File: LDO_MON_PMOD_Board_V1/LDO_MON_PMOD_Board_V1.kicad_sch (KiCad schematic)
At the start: 49 parts, among them J1 Conn_01x03, P1 PMOD-Device-x2-Type-Generic-A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, P2 PMOD-Device-x2-Type-Generic-A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, U1 LT3074AV#PBF, U2 LT3074AV#PBF

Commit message: Schematic and PCB Updates.
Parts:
- added C28, C29, C30, C31, C33, C47: 100n, Capacitor_SMD:C_0402_1005Metric, symbol Device:C_Small
- added C32: 4u7, Capacitor_SMD:C_0603_1608Metric, symbol Device:C_Small
- added C34, C37, C40, C43: 47n, Capacitor_SMD:C_0402_1005Metric, symbol Device:C_Small
- added C35, C36, C38, C39, C41, C42, C44, C45: 4n7, Capacitor_SMD:C_0402_1005Metric, symbol Device:C_Small
- added C46: 10n, Capacitor_SMD:C_0402_1005Metric, symbol Device:C_Small
- added C48: 10u, Capacitor_SMD:C_0603_1608Metric, symbol Device:C_Small
- added C49: 1u, Capacitor_SMD:C_0402_1005Metric, symbol Device:C_Small
- added J2: 2-Pin Harwin, Connector_PinHeader_2.54mm:PinHeader_1x02_P2.54mm_Vertical, symbol Connector_Generic:Conn_01x02
- added J3: Conn_01x04, Connector_Phoenix_MC:PhoenixContact_MC_1,5_4-G-3.5_1x04_P3.50mm_Horizontal, symbol Connector_Generic:Conn_01x04
- added JP1, JP2, JP3: SolderJumper_3_Open, Jumper:SolderJumper-3_P1.3mm_Open_RoundedPad1.0x1.5mm, symbol Jumper:SolderJumper_3_Open
- added R17, R20, R21, R23, R24, R25, R37, R38: 10k, Resistor_SMD:R_0402_1005Metric, symbol Device:R
- added R18, R19: 1k, Resistor_SMD:R_0402_1005Metric, symbol Device:R
- added R26, R36, R8: 0R, Resistor_SMD:R_0402_1005Metric, symbol Device:R
- added R27, R28, R29, R30, R31, R32, R33, R34: 4k99, Resistor_SMD:R_0402_1005Metric, symbol Device:R
- added R35, R39: 15mR, Resistor_SMD:R_2512_6332Metric, symbol Device:R
- added R40: 100R, Resistor_SMD:R_0402_1005Metric, symbol Device:R
- added R9: 50k, Resistor_SMD:R_0402_1005Metric, symbol Device:R
- added U3: MAX6373, Package_TO_SOT_SMD:SOT-23-8, symbol Power_Supervisor:MAX6373
- added U4: 74LVC1G175, Package_TO_SOT_SMD:SOT-563, symbol 74xGxx:74LVC1G175
- added U5: PAC1944x-x4MX, Package_DFN_QFN:VQFN-16-1EP_3x3mm_P0.5mm_EP1.1x1.1mm, symbol Sensor_Energy:PAC1944x-x4MX
- added U6: 74LVC1G08, Package_TO_SOT_SMD:Texas_R-PDSO-G5_DCK-5, symbol 74xGxx:74LVC1G08
- added U7: AD5272BCP, Package_CSP:LFCSP-WD-10-1EP_3x3mm_P0.5mm_EP1.64x2.38mm, symbol Potentiometer_Digital:AD5272BCP
- C1, C14, C15, C17, C18, C19, C20, C21, C23, C24, C26, C27, C5: footprint (none) -> Capacitor_SMD:C_0402_1005Metric
- C10, C12, C4, C7: footprint (none) -> Capacitor_SMD:C_1210_3225Metric
- C11, C13, C16, C2, C22, C25, C3, C8, C9: footprint (none) -> Capacitor_SMD:C_0603_1608Metric
- C6: footprint (none) -> Capacitor_SMD:CP_Elec_8x10
- J1: value Conn_01x03 -> 3-Pin Harwin; footprint Connector:Tag-Connect_TC2030-IDC-FP_2x03_P1.27mm_Vertical -> Connector_PinHeader_2.54mm:PinHeader_1x03_P2.54mm_Vertical
- P1, P2: footprint pmod-conn_6x2:pmod_pin_array_6x2 -> klib_connectors:pmod_pin_array_6x2
- R1, R11, R12, R3, R5: footprint (none) -> Resistor_SMD:R_0402_1005Metric
- R13: value 1k -> 69k8; footprint (none) -> Resistor_SMD:R_0402_1005Metric
- R14, R2: value 1k -> 261k; footprint (none) -> Resistor_SMD:R_0402_1005Metric
- R15, R16: footprint (none) -> Resistor_SMD:R_2512_6332Metric
- R4: value 1k -> 47k5; footprint (none) -> Resistor_SMD:R_0402_1005Metric
- R6, R7: value 10k -> 4k7; footprint (none) -> Resistor_SMD:R_0402_1005Metric
- TP1, TP2, TP3, TP4: footprint Package_TO_SOT_SMD:SOT-23-5 -> TestPoint:TestPoint_Pad_1.0x1.0mm
- U1, U2: footprint Package_DFN_QFN:DFN-6-1EP_2x2mm_P0.5mm_EP0.6x1.37mm -> klib_logic:LT3074AV#PBF
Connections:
- net 3V3_PMOD: now also C29.1, C30.1, C31.1, C32.1, C33.1, C46.1, C47.1, C48.1, J2.1 (Pin_1), JP1.3 (B), JP2.3 (B), JP3.3 (B), R17.1, R18.1, R23.1, R24.1, R25.1, R37.1, U3.8 (VCC), U4.3 (D), U4.5 (VCC), U5.2 (V_{DD}), U6.5 (VCC), U7.1 (VDD)
- net ENABLE: now also J2.2 (Pin_2), R18.2, R40.1, U6.4; no longer U2.22 (EN)
- net EXT_VBIAS: now also J3.1 (Pin_1)
- net GND: now also C28.2, C29.2, C30.2, C31.2, C32.2, C33.2, C35.2, C36.2, C38.2, C39.2, C41.2, C42.2, C44.2, C45.2, C46.2, C47.2, C48.2, C49.2, J3.4 (Pin_4), JP1.1 (A), JP2.1 (A), JP3.1 (A), R19.2, R20.2, R21.2, R26.2, R38.2, R8.2, R9.2, U3.2 (GND), U4.2 (GND), U5.17 (EP), U5.3 (GND), U6.3 (GND), U7.11 (VSS), U7.3 (W), U7.4 (VSS), U7.6 (GND)
- net OUT_1: now also R28.2
- net OUT_2: now also R29.2
- net SCL: now also U5.4 (SCL), U7.9 (SCL)
- net SDA: now also U5.5 (SDA), U7.8 (SDA)
- net SET_RES_NODE: now also R36.2, R8.1
- net CNTRL: now reaches P2.7 (P7)
- net CNTRL: now also R20.1, U6.2
- net WDI: now reaches P2.8 (P8)
- net WDI: now also R19.1, U3.1 (WDI), U4.1 (C)
- net PAC_EN: now reaches P1.1 (P1)
- net PAC_EN: now also R23.2, U5.16 (~{PWRDN})
- net SLOW: now reaches P1.2 (P2)
- net SLOW: now also R24.2, U5.1 (SLOW)
- net GPIO: now reaches P1.3 (P3)
- net GPIO: now also R25.2, U5.15 (GPIO)
- net DP_RST_N: now reaches P1.4 (P4)
- net DP_RST_N: now also R37.2, U7.7 (~{RESET})
- net V_COMB renamed SENSE_1_N
- net SENSE_1_N: now also R27.2, R30.2, R31.2, R39.1
- net V_IN renamed SENSE_4_N
- net SENSE_4_N: now also R34.2, R35.1
- new net: C37.1, C38.1, R29.1, U5.13 (SENSE2+)
- new net: C37.2, C39.1, R30.1, U5.14 (SENSE2-)
- new net: R38.1, U7.10 (ADDR)
- new net: R36.1, R9.1, U7.2 (A)
- new net: C49.1, U7.5 (EXT_CAP)
- new net: C28.1, R17.2, U3.7 (~{WDO}), U4.6 (~{CLR})
- new net: R40.2, U2.22 (EN)
- new net: C43.1, C44.1, R33.1, U5.10 (SENSE4+)
- new net: C34.2, C36.1, R27.1, U5.12 (SENSE1-)
- new net: C34.1, C35.1, R28.1, U5.11 (SENSE1+)
- new net: C40.2, C42.1, R32.1, U5.7 (SENSE3-)
- new net: JP2.2 (C), U3.5 (SET1)
- new net: R21.1, U4.4 (Q), U6.1
- new net: C43.2, C45.1, R34.1, U5.9 (SENSE4-)
- new net: JP3.2 (C), U3.6 (SET2)
- new net: C40.1, C41.1, R31.1, U5.8 (SENSE3+)
- new net: JP1.2 (C), U3.4 (SET0)
- new net: R26.1, U5.6 (ADDRSEL)
- new net SENSE_3_N: J3.2 (Pin_2), R32.2, R39.2
- new net SENSE_4_P: J3.3 (Pin_3), R33.2, R35.2
- no-connect marks 2 -> 9
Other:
- note added: "ADDRESS: 0x10"
- note added: "ADDRESS: 0x2F"
- note added: "ADDRESS: 0x6D"
- note added: "ADDRESS: 0x6F"
- note added: "DNF"
- note added: "LOCATE CLOSE TO REGULATORS"
- note added: "NOTE: AD5272 VERSION - 50K NOMINAL RESISTANCE"
- note added: "WATCHDOG CIRCUIT DECOUPLING"
- note added: "WSL25122L000FED"
- note added: "WSL2512R0150FEA"
- moved on the sheet: C1, C10, C11, C12, C13, C14, C15, C16, C17, C18, C19, C2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

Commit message: Schematic/PCB Updates.
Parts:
- removed P2: PMOD-Device-x2-Type-Generic-Alt, klib_connectors:pmod_pin_array_6x2, symbol klib_connectors:PMOD-Device-x2-Type-Generic-Alt
- added C50: 47u, Capacitor_SMD:C_1210_3225Metric, symbol Device:C_Small
- U4: footprint Package_TO_SOT_SMD:SOT-563 -> Package_TO_SOT_SMD:SOT-23-6
- U6: footprint Package_TO_SOT_SMD:Texas_R-PDSO-G5_DCK-5 -> Package_TO_SOT_SMD:Texas_R-PDSO-N5_DRL-5
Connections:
- net ALERT_N: now also P1.3 (P3)
- net CNTRL: now also P1.9 (P9)
- net GND: now also C50.2
- net GPIO: no longer P1.3 (P3)
- net SCL: now also P1.7 (P7)
- net SDA: now also P1.8 (P8)
- net SENSE_4_N: now also C50.1
- net WDI: now also P1.10 (P10)
- no-connect marks 9 -> 2
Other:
- moved on the sheet: C22, C23, C24, C46, C47, C48, C49, C6, C7, C8, J1, R36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

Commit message: PCB Updates.
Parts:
- added C51, C52: 100n, Capacitor_SMD:C_0402_1005Metric, symbol Device:C_Small
- added D1, D2: LED, LED_SMD:LED_0402_1005Metric, symbol Device:LED
- added Q1: MMBT3904, Package_TO_SOT_SMD:SOT-23, symbol Transistor_BJT:MMBT3904
- added R10, R41, R43: 4k7, Resistor_SMD:R_0402_1005Metric, symbol Device:R
- added R22: 200k, Resistor_SMD:R_0402_1005Metric, symbol Device:R
- added R42, R44: 1k, Resistor_SMD:R_0402_1005Metric, symbol Device:R
- added U8: PCA9306, Package_SO:VSSOP-8_2.3x2mm_P0.5mm, symbol Interface:PCA9306
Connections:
- net 3V3_PMOD: now also C52.1, D1.2 (A), D2.2 (A), R10.1, R41.1, U8.2 (VREF1)
- net BIAS: now also R22.1
- net CNTRL: now also P1.4 (P4); no longer P1.9 (P9)
- net DP_RST_N: now also P1.7 (P7); no longer P1.4 (P4)
- net ENABLE: now also R43.1
- net GND: now also C51.2, C52.2, Q1.2 (E), R42.2, U8.1 (GND)
- net SCL: now also P1.8 (P8), R10.2, U8.3 (SCL1); no longer P1.7 (P7), R6.2, U1.4 (SCL), U2.4 (SCL)
- net SDA: now also P1.9 (P9), R41.2, U8.4 (SDA1); no longer P1.8 (P8), R7.2, U1.5 (SDA), U2.5 (SDA)
- net SENSE_2_P_FILT: now reaches C37.1, C38.1, R29.1
- net SENSE_2_P_FILT: now also U5.8 (SENSE3+); no longer U5.13 (SENSE2+)
- net SENSE_2_N_FILT: now reaches C37.2, C39.1, R30.1
- net SENSE_2_N_FILT: now also U5.7 (SENSE3-); no longer U5.14 (SENSE2-)
- net SENSE_4_P_FILT: now reaches C43.1, C44.1, R33.1
- net SENSE_4_P_FILT: now also U5.13 (SENSE2+); no longer U5.10 (SENSE4+)
- net SENSE_1_N_FILT: now reaches C34.2, C36.1, R27.1
- net SENSE_1_N_FILT: now also U5.9 (SENSE4-); no longer U5.12 (SENSE1-)
- net SENSE_1_P_FILT: now reaches C34.1, C35.1, R28.1
- net SENSE_1_P_FILT: now also U5.10 (SENSE4+); no longer U5.11 (SENSE1+)
- net SENSE_3_N_FILT: now reaches C40.2, C42.1, R32.1
- net SENSE_3_N_FILT: now also U5.12 (SENSE1-); no longer U5.7 (SENSE3-)
- net SENSE_4_N_FILT: now reaches C43.2, C45.1, R34.1
- net SENSE_4_N_FILT: now also U5.14 (SENSE2-); no longer U5.9 (SENSE4-)
- net SENSE_3_P_FILT: now reaches C40.1, C41.1, R31.1
- net SENSE_3_P_FILT: now also U5.11 (SENSE1+); no longer U5.8 (SENSE3+)
- new net: D1.1 (K), R42.1
- new net: Q1.1 (B), R43.2
- new net: D2.1 (K), R44.1
- new net: Q1.3 (C), R44.2
- new net: C51.1, R22.2, U8.7 (VREF2), U8.8 (EN)
- new net SCL_HV: R6.2, U1.4 (SCL), U2.4 (SCL), U8.6 (SCL2)
- new net SDA_HV: R7.2, U1.5 (SDA), U2.5 (SDA), U8.5 (SDA2)
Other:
- moved on the sheet: C34, C35, C36, C37, C38, C39, C40, C41, C42, C43, C44, C45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

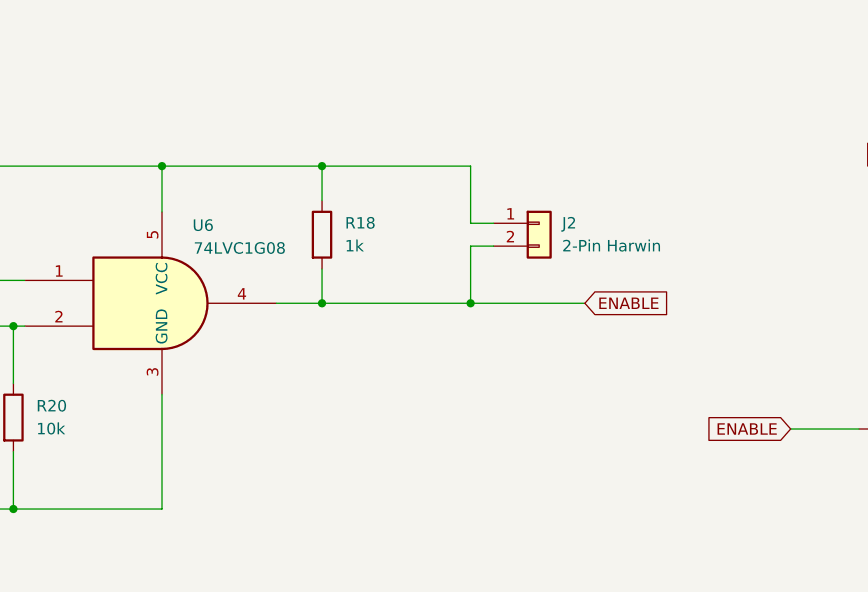
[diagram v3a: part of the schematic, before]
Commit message: Fixed problem with watchdog enable bypass. Updated schematic/PCB/gerbers. No change to placement or BOM.
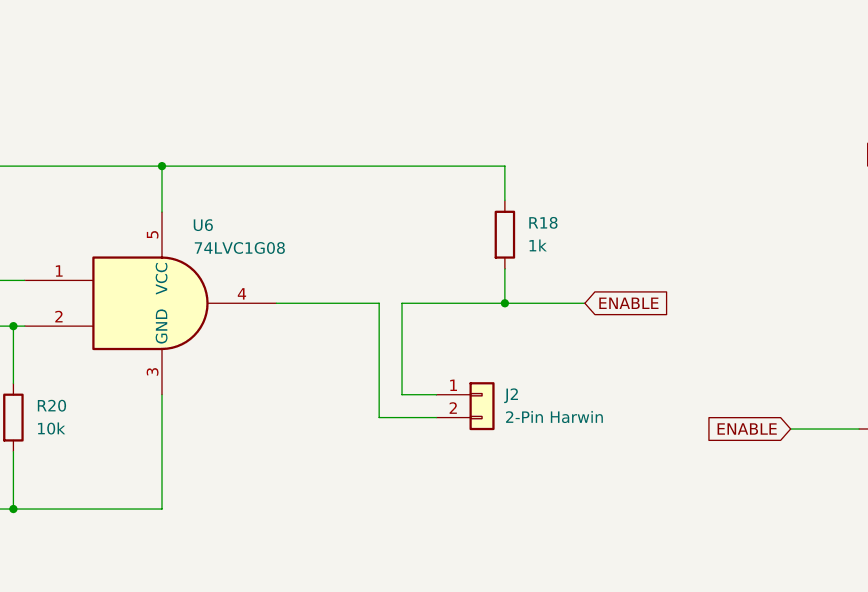
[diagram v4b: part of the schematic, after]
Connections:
- net 3V3_PMOD: no longer J2.1 (Pin_1)
- net ENABLE: now also J2.1 (Pin_1); no longer J2.2 (Pin_2), U6.4
- new net: J2.2 (Pin_2), U6.4
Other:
- moved on the sheet: J2, R18
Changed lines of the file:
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@@
 	)
 	(junction
-		(at 203.2 172.72)
-		(diameter 0)
-		(color 0 0 0 0)
-	)
-	(junction
 		(at 270.51 106.68)
 		(diameter 0)
@@
 	)
 	(junction
-		(at 237.49 187.96)
-		(diameter 0)
-		(color 0 0 0 0)
-	)
-	(junction
 		(at 222.25 264.16)
 		(diameter 0)
@@
 	)
 	(junction
-		(at 220.98 187.96)
-		(diameter 0)
-		(color 0 0 0 0)
-	)
-	(junction
 		(at 190.5 116.84)
 		(diameter 0)
@@
 	)
 	(junction
-		(at 220.98 172.72)
-		(diameter 0)
-		(color 0 0 0 0)
-	)
-	(junction
 		(at 471.17 320.04)
 		(diameter 0)
@@
 	)
 	(junction
+		(at 203.2 172.72)
+		(diameter 0)
+		(color 0 0 0 0)
+	)
+	(junction
 		(at 414.02 149.86)
 		(diameter 0)
@@
 		(color 0 0 0 0)
 	)
+	(junction
+		(at 241.3 187.96)
+		(diameter 0)
+		(color 0 0 0 0)
+	)
 	(no_connect
 		(at 467.36 54.61)
@@
 	(wire
 		(pts
+			(xy 203.2 172.72) (xy 241.3 172.72)
+		)
+		(stroke
+			(width 0)
+			(type default)
+		)
+	)
+	(wire
+		(pts
 			(xy 217.17 335.28) (xy 217.17 337.82)
 		)
@@
 	(wire
 		(pts
-			(xy 237.49 187.96) (xy 250.19 187.96)
-		)
-		(stroke
-			(width 0)
-			(type default)
-		)
-	)
-	(wire
-		(pts
 			(xy 243.84 314.96) (xy 254 314.96)
 		)
@@
 	(wire
 		(pts
-			(xy 220.98 184.15) (xy 220.98 187.96)
+			(xy 241.3 184.15) (xy 241.3 187.96)
 		)
 		(stroke
@@
 	(wire
 		(pts
-			(xy 220.98 176.53) (xy 220.98 172.72)
+			(xy 241.3 176.53) (xy 241.3 172.72)
 		)
 		(stroke
@@
 	(wire
 		(pts
+			(xy 233.68 200.66) (xy 227.33 200.66)
+		)
+		(stroke
+			(width 0)
+			(type default)
+		)
+	)
+	(wire
+		(pts
 			(xy 462.28 139.7) (xy 462.28 142.24)
 		)
@@
 	(wire
 		(pts
+			(xy 227.33 200.66) (xy 227.33 187.96)
+		)
+		(stroke
+			(width 0)
+			(type default)
+		)
+	)
+	(wire
+		(pts
 			(xy 129.54 279.4) (xy 139.7 279.4)
 		)
@@
 	(wire
 		(pts
+			(xy 241.3 187.96) (xy 250.19 187.96)
+		)
+		(stroke
+			(width 0)
+			(type default)
+		)
+	)
+	(wire
+		(pts
 			(xy 351.79 311.15) (xy 351.79 316.23)
 		)
@@
 	(wire
 		(pts
-			(xy 220.98 187.96) (xy 237.49 187.96)
-		)
-		(stroke
-			(width 0)
-			(type default)
-		)
-	)
-	(wire
-		(pts
 			(xy 129.54 210.82) (xy 107.95 210.82)
 		)
@@
 	(wire
 		(pts
-			(xy 240.03 179.07) (xy 237.49 179.07)
-		)
-		(stroke
-			(width 0)
-			(type default)
-		)
-	)
-	(wire
-		(pts
 			(xy 195.58 114.3) (xy 193.04 114.3)
 		)
@@
 	(wire
 		(pts
-			(xy 220.98 172.72) (xy 237.49 172.72)
+			(xy 440.69 57.15) (xy 440.69 55.88)
 		)
 		(stroke
@@
 	(wire
 		(pts
-			(xy 440.69 57.15) (xy 440.69 55.88)
+			(xy 510.54 223.52) (xy 510.54 228.6)
 		)
 		(stroke
@@
 	(wire
 		(pts
-			(xy 510.54 223.52) (xy 510.54 228.6)
+			(xy 229.87 198.12) (xy 229.87 187.96)
 		)
 		(stroke
@@
 	(wire
 		(pts
-			(xy 220.98 172.72) (xy 203.2 172.72)
-		)
-		(stroke
-			(width 0)
-			(type default)
-		)
-	)
-	(wire
-		(pts
 			(xy 222.25 264.16) (xy 222.25 266.7)
 		)
@@
 	(wire
 		(pts
-			(xy 240.03 181.61) (xy 237.49 181.61)
+			(xy 73.66 52.07) (xy 80.01 52.07)
 		)
 		(stroke
@@
 	(wire
 		(pts
-			(xy 73.66 52.07) (xy 80.01 52.07)
+			(xy 129.54 284.48) (xy 139.7 284.48)
 		)
 		(stroke
@@
 	(wire
 		(pts
-			(xy 129.54 284.48) (xy 139.7 284.48)
+			(xy 233.68 198.12) (xy 229.87 198.12)
 		)
 		(stroke
@@
 	(wire
 		(pts
-			(xy 237.49 179.07) (xy 237.49 172.72)
+			(xy 173.99 204.47) (xy 173.99 210.82)
 		)
 		(stroke
@@
 	(wire
 		(pts
-			(xy 173.99 204.47) (xy 173.99 210.82)
+			(xy 440.69 274.32) (xy 452.12 274.32)
 		)
 		(stroke
@@
 	(wire
 		(pts
-			(xy 440.69 274.32) (xy 452.12 274.32)
+			(xy 229.87 187.96) (xy 241.3 187.96)
 		)
 		(stroke
@@
 	(wire
 		(pts
-			(xy 237.49 181.61) (xy 237.49 187.96)
-		)
-		(stroke
-			(width 0)
-			(type default)
-		)
-	)
-	(wire
-		(pts
 			(xy 480.06 320.04) (xy 481.33 320.04)
 		)
@@
 	(wire
 		(pts
-			(xy 215.9 187.96) (xy 220.98 187.96)
+			(xy 92.71 127) (xy 71.12 127)
 		)
 		(stroke
@@
 	(wire
 		(pts
-			(xy 92.71 127) (xy 71.12 127)
+			(xy 227.33 353.06) (xy 227.33 355.6)
 		)
 		(stroke
@@
 	(wire
 		(pts
-			(xy 227.33 353.06) (xy 227.33 355.6)
+			(xy 73.66 39.37) (xy 80.01 39.37)
 		)
 		(stroke
@@
 	(wire
 		(pts
-			(xy 73.66 39.37) (xy 80.01 39.37)
+			(xy 463.55 342.9) (xy 472.44 342.9)
 		)
 		(stroke
@@
 	(wire
 		(pts
-			(xy 463.55 342.9) (xy 472.44 342.9)
+			(xy 190.5 86.36) (xy 190.5 88.9)
 		)
 		(stroke
@@
 	(wire
 		(pts
-			(xy 190.5 86.36) (xy 190.5 88.9)
+			(xy 318.77 290.83) (xy 318.77 298.45)
 		)
 		(stroke
@@
 	(wire
 		(pts
-			(xy 318.77 290.83) (xy 318.77 298.45)
+			(xy 227.33 187.96) (xy 215.9 187.96)
 		)
 		(stroke
@@
 	(symbol
 		(lib_id "Device:R")
-		(at 220.98 180.34 0)
+		(at 241.3 180.34 0)
 		(unit 1)
 		(body_style 1)
@@
 		(fields_autoplaced yes)
 		(property "Reference" "R18"
-			(at 223.52 179.0699 0)
+			(at 243.84 179.0699 0)
 			(show_name no)
 			(do_not_autoplace no)
@@
 		)
 		(property "Value" "1k"
-			(at 223.52 181.6099 0)
+			(at 243.84 181.6099 0)
 			(show_name no)
 			(do_not_autoplace no)
@@
 		)
 		(property "Footprint" "Resistor_SMD:R_0402_1005Metric"
-			(at 219.202 180.34 90)
+			(at 239.522 180.34 90)
 			(hide yes)
 			(show_name no)
@@
 		)
 		(property "Datasheet" ""
-			(at 220.98 180.34 0)
+			(at 241.3 180.34 0)
 			(hide yes)
 			(show_name no)
@@
 		)
 		(property "Description" "Resistor"
-			(at 220.98 180.34 0)
+			(at 241.3 180.34 0)
 			(hide yes)
 			(show_name no)
@@
 	(symbol
 		(lib_id "Connector_Generic:Conn_01x02")
-		(at 245.11 179.07 0)
+		(at 238.76 198.12 0)
 		(unit 1)
 		(body_style 1)
@@
 		(fields_autoplaced yes)
 		(property "Reference" "J2"
-			(at 247.65 179.0699 0)
+			(at 241.3 198.1199 0)
 			(show_name no)
 			(do_not_autoplace no)
@@
 		)
 		(property "Value" "2-Pin Harwin"
-			(at 247.65 181.6099 0)
+			(at 241.3 200.6599 0)
 			(show_name no)
 			(do_not_autoplace no)
@@
 		)
 		(property "Footprint" "Connector_PinHeader_2.54mm:PinHeader_1x02_P2.54mm_Vertical"
-			(at 245.11 179.07 0)
+			(at 238.76 198.12 0)
 			(hide yes)
 			(show_name no)
@@
 		)
 		(property "Datasheet" ""
-			(at 245.11 179.07 0)
+			(at 238.76 198.12 0)
 			(hide yes)
 			(show_name no)
@@
 		)
 		(property "Description" "Generic connector, single row, 01x02, script generated (kicad-library-utils/schlib/autogen/connector/)"
-			(at 245.11 179.07 0)
+			(at 238.76 198.12 0)
 			(hide yes)
 			(show_name no)

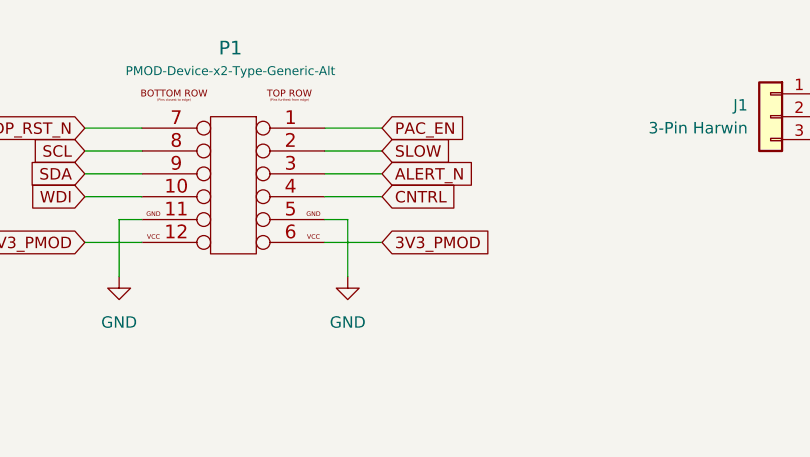
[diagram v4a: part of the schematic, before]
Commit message: Fixed/removed alert_n flag at wrong voltage potential.
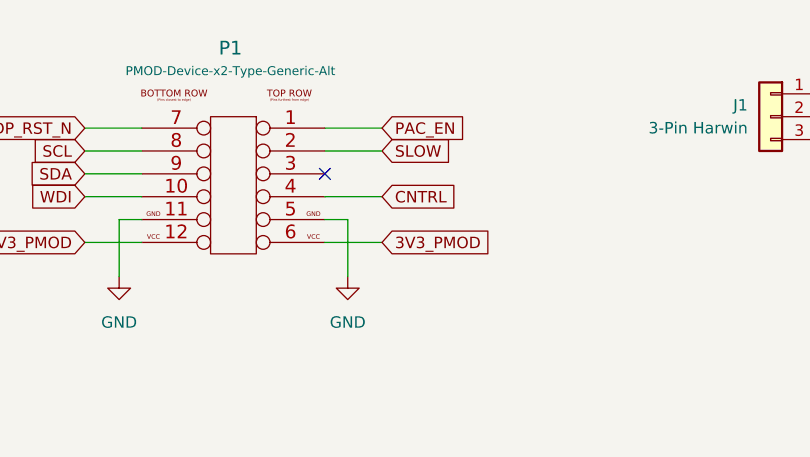
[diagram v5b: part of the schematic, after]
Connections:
- net ALERT_N: no longer P1.3 (P3)
- no-connect marks 2 -> 3
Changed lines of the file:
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@@
 	)
 	(no_connect
+		(at 73.66 44.45)
+	)
+	(no_connect
 		(at 467.36 161.29)
 	)
@@
 	(wire
 		(pts
-			(xy 73.66 44.45) (xy 80.01 44.45)
-		)
-		(stroke
-			(width 0)
-			(type default)
-		)
-	)
-	(wire
-		(pts
 			(xy 538.48 148.59) (xy 538.48 151.13)
 		)
@@
 			)
 		)
-	)
-	(global_label "ALERT_N"
-		(shape input)
-		(at 80.01 44.45 0)
-		(fields_autoplaced yes)
-		(effects
-			(font
-				(size 1.27 1.27)
-			)
-			(justify left)
-		)
-		(property "Intersheetrefs" "${INTERSHEET_REFS}"
-			(at 90.7966 44.45 0)
-			(hide yes)
-			(show_name no)
-			(do_not_autoplace no)
-			(effects
-				(font
-					(size 1.27 1.27)
-				)
-				(justify left)
-			)
-		)
